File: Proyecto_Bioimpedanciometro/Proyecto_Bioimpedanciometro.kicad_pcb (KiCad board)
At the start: 2 copper layers, 63.5 x 34.3 mm, 28 parts, among them IC1 ATMEGA328P-A, P1 CONN_01X10, P2 CONN_01X04, U1 ADG849, U2 AD8606, U3 APD3339, Y1 Crystal_Small

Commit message: Segunda Version
Empieza PCB
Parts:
- removed C11: C, Capacitors_SMD:C_0805_HandSoldering
- added P3: CONN_01X04, Huellas:Pin_Header_Straight_1x04_Pitch2.54mm_Completo, F.Cu at (175.3, 144.7)
- added R10: R, Resistors_SMD:R_0805_HandSoldering, F.Cu at (175.3, 144.7)
- P1: value CONN_01X10 -> CONN_01X09; footprint Huellas:Pin_Header_Straight_1x10_Pitch2.54mm_Completo -> Huellas:Pin_Header_Straight_1x09_Pitch2.54mm_Completo
- P2: value CONN_01X04 -> CONN_01X03; footprint Huellas:Pin_Header_Straight_1x04_Pitch2.54mm_Completo -> Huellas:Pin_Header_Straight_1x03_Pitch2.54mm_Completo
- moved C7 31.6 mm to (153.7, 111.8), turned to 270 degrees
- moved C9 17.0 mm to (170.9, 111.8), turned to 180 degrees
- moved R9 15.5 mm to (155.4, 128.8)
- moved R7 5.61 mm to (173.5, 127.8)
- moved C4 5.36 mm to (173.5, 125.5)
- moved Y1 4.58 mm to (166.6, 110.2)
- moved IC1 4.33 mm to (159.8, 112.5)
- moved BIO1 4.33 mm to (159.5, 122.2)
- moved P1 2.74 mm to (148.1, 102.9)
- moved C10 1.52 mm to (170.9, 108.7)
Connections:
- C7 pad 1: +3V3 -> /3V3
- C9 pad 1: +3V3 -> GND
- C9 pad 2: GND -> Net-(C9-Pad2)
- IC1 pad 18: +3V3 -> /3V3
- IC1 pad 4: +3V3 -> /3V3
- IC1 pad 6: +3V3 -> /3V3
- IC1 pad 7: Net-(C10-Pad2) -> Net-(C9-Pad2)
- IC1 pad 8: Net-(C11-Pad2) -> Net-(C10-Pad2)
- P1 pad 1: /RXD -> /MOSI
- P1 pad 2: /TXD -> /MISO
- P1 pad 3: /ADC0 -> /SCK
- P1 pad 4: /ADC1 -> /3V3
- P1 pad 5: /ADC2 -> GND
- P1 pad 6: /ADC3 -> /ADC0
- P1 pad 7: /MOSI -> /ADC1
- P1 pad 8: /MISO -> /ADC2
- P1 pad 9: /SCK -> /ADC3
- P2 pad 1: /V_FUENTE -> /RXD
- P2 pad 2: /Z_UK -> /TXD
- P2 pad 3: /IN_A -> /RESET
- Y1 pad 1: Net-(C10-Pad2) -> Net-(C9-Pad2)
- Y1 pad 2: Net-(C11-Pad2) -> Net-(C10-Pad2)
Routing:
- net Net-(C4-Pad2): track 18.1 -> 0.00 mm
- net /VIN_AD5933: track 14.5 -> 0.96 mm
- net GND: track 0.00 -> 10.8 mm
- net /OUT_B: track 10.7 -> 0.00 mm
- net /3V3: track 0.00 -> 7.70 mm
- net /SDA: track 0.00 -> 7.48 mm
- net Net-(BIO1-Pad5): track 6.93 -> 0.00 mm
- net Net-(C9-Pad2): track 0.00 -> 6.44 mm
- net /SCL: track 0.00 -> 6.14 mm
- net Net-(BIO1-Pad4): track 4.45 -> 0.00 mm
- net Net-(BIO1-Pad6): track 3.51 -> 0.00 mm
- net Net-(C11-Pad2): track 3.37 -> 0.00 mm
- net /IN_A: track 3.13 -> 0.00 mm
- net Net-(C10-Pad2): track 3.25 -> 6.12 mm
- net /MISO: track 0.00 -> 1.52 mm

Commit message: Tercera Version
Revisar conexion bajo el micro, se hizo teniendo en cuenta simetria
segun lo hablado.
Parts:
- moved P2 37.2 mm to (167.4, 115.8)
- moved P3 35.3 mm to (203.6, 123.7)
- moved R10 31.2 mm to (196.6, 121.9)
- moved C8 26.8 mm to (171.2, 117.0), turned to 270 degrees
- moved R5 23.7 mm to (173.1, 127.9), turned to 270 degrees
- moved C2 22.4 mm to (181.4, 124.6), turned to 270 degrees
- moved R8 22.1 mm to (170.4, 127.9), turned to 270 degrees
- moved R7 19.8 mm to (153.7, 127.8)
- moved U2 12.6 mm to (176.9, 124.8), turned to 90 degrees
- moved C6 7.82 mm to (173.7, 117.1), turned to 270 degrees
- moved C4 6.56 mm to (167.0, 126.5)
- moved R9 6.37 mm to (152.4, 123.2), turned to 270 degrees
- moved BIO1 0.51 mm to (159.5, 122.7)
- moved C10 0.25 mm to (171.2, 108.7)
- moved C9 0.25 mm to (171.2, 111.8)
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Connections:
- P2 pad 1: /RXD -> /TXD
- P2 pad 2: /TXD -> /RXD
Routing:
- net /VIN_AD5933: track 0.96 -> 20.4 mm
- net Net-(BIO1-Pad6): track 0.00 -> 15.3 mm
- net /MOSI: track 0.00 -> 12.8 mm
- net /3V3: track 7.70 -> 19.6 mm
- net GND: track 10.8 -> 21.8 mm
- net /ADC2: track 0.00 -> 10.8 mm
- net Net-(C4-Pad2): track 0.00 -> 10.3 mm
- net /RESET: track 0.00 -> 10.1 mm
- net /MISO: track 1.52 -> 10.8 mm
- net /ADC1: track 0.00 -> 8.84 mm
- net /SCK: track 0.00 -> 8.42 mm
- net Net-(BIO1-Pad5): track 0.00 -> 8.36 mm
- net /ADC0: track 0.00 -> 8.12 mm
- net /RXD: track 0.00 -> 7.55 mm
- net /TXD: track 0.00 -> 7.12 mm
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
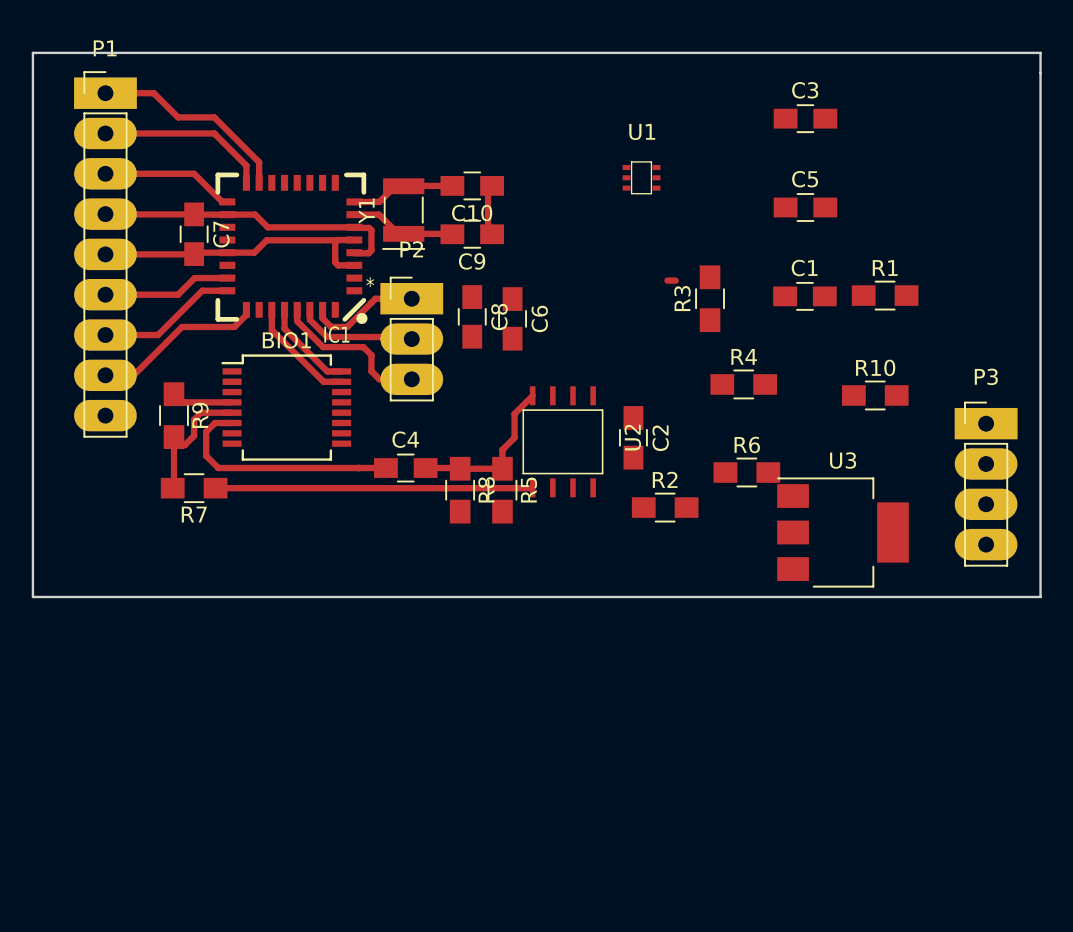
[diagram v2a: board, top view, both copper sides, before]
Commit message: Cuarta Versión
Revisar todo el diseño y errores mas importantes
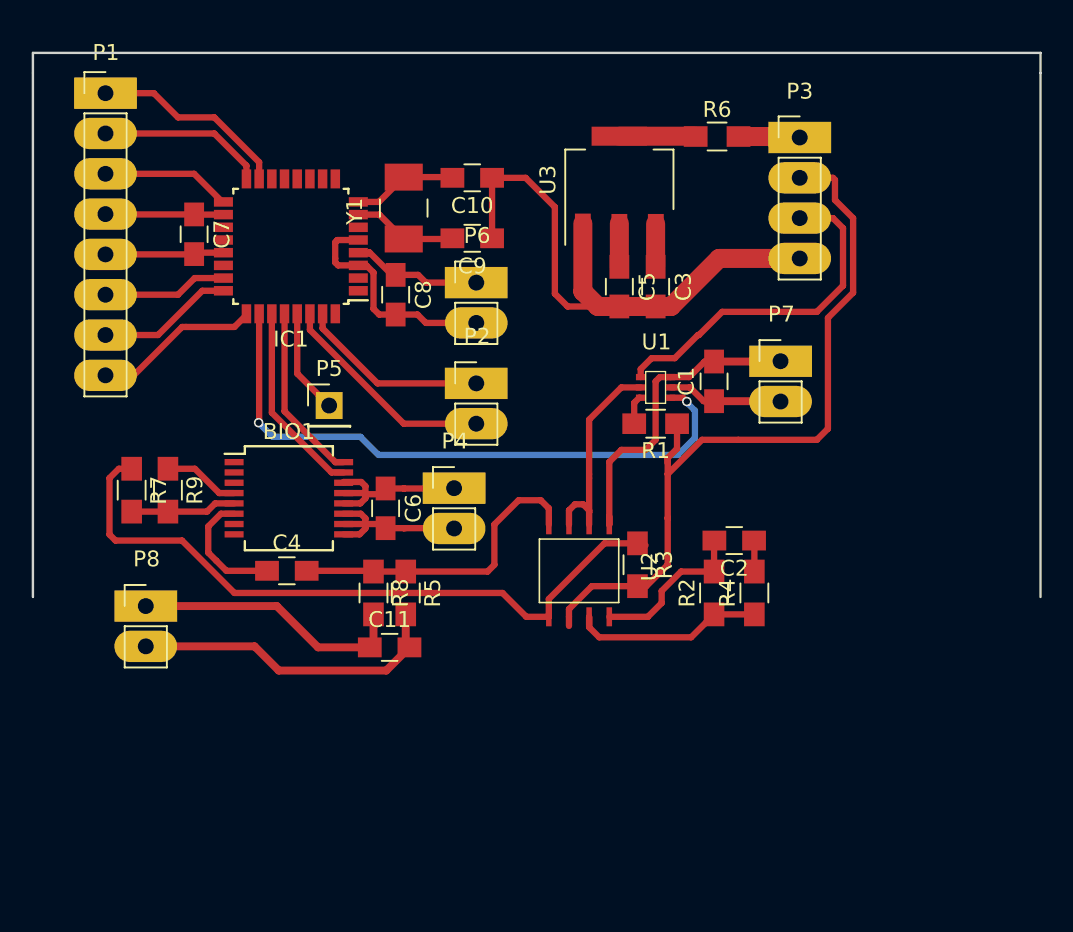
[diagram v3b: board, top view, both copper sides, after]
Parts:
- removed R10: R, Resistors_SMD:R_0805_HandSoldering
- added C11: 0,1uF, Capacitors_SMD:C_0805_HandSoldering, F.Cu at (166.0, 137.8)
- added P4: CONN_01X02, Huellas:Pin_Header_Straight_1x02_Pitch2.54mm_Completo, F.Cu at (170.1, 127.8)
- added P5: CONN_01X01, Pin_Headers:Pin_Header_Straight_1x01_Pitch2.54mm, F.Cu at (162.2, 122.6)
- added P6: CONN_01X02, Huellas:Pin_Header_Straight_1x02_Pitch2.54mm_Completo, F.Cu at (171.4, 114.8)
- added P7: CONN_01X02, Huellas:Pin_Header_Straight_1x02_Pitch2.54mm_Completo, F.Cu at (190.6, 119.8)
- added P8: CONN_01X02, Huellas:Pin_Header_Straight_1x02_Pitch2.54mm_Completo, F.Cu at (150.6, 135.2)
- C1, C2, C7, C8: value C -> 0,1uF
- C10, C9: value C -> 18pF
- C3, C5: value C -> 1uF
- C4: value C -> 47nF
- IC1: footprint Universal:TQFP32 -> Housings_QFP:LQFP-32_7x7mm_Pitch0.8mm
- P1: value CONN_01X09 -> CONN_01X08; footprint Huellas:Pin_Header_Straight_1x09_Pitch2.54mm_Completo -> Huellas:Pin_Header_Straight_1x08_Pitch2.54mm_Completo
- P2: value CONN_01X03 -> CONN_01X02; footprint Huellas:Pin_Header_Straight_1x03_Pitch2.54mm_Completo -> Huellas:Pin_Header_Straight_1x02_Pitch2.54mm_Completo
- R1: value R -> Rcal
- R2, R4, R5, R8: value R -> 50k
- R3: value R -> Rfb
- R6: value R -> 0
- R7, R9: value R -> 20k
- U3: footprint TO_SOT_Packages_SMD:SOT-223 -> Huellas:SOT-223_ADP3339
- Y1: footprint Crystals:Resonator_SMD_muRata_CDSCB-2pin_4.5x2.0mm -> Huellas:AMB3_Crystal_5mm_x_3,2mm_16M
- moved U3 26.3 mm to (180.5, 108.3), turned to 90 degrees
- moved P3 21.5 mm to (191.8, 105.7)
- moved R6 21.3 mm to (186.6, 105.6)
- moved R3 17.4 mm to (181.6, 132.6), turned to 270 degrees
- moved R1 16.6 mm to (182.8, 123.7), turned to 180 degrees
- moved C6 14.4 mm to (165.7, 129.0)
- moved C3 14.2 mm to (182.8, 115.1), turned to 270 degrees
- moved U1 13.2 mm to (182.8, 121.4)
- moved R4 13.2 mm to (189.0, 134.4), turned to 90 degrees
- moved C5 12.7 mm to (180.5, 115.1), turned to 270 degrees
- moved C4 9.90 mm to (159.5, 133.0)
- moved C2 9.07 mm to (187.7, 131.1), turned to 180 degrees
- moved R5 8.89 mm to (167.0, 134.4)
- moved R8 8.47 mm to (165.0, 134.4)
- moved U2 8.19 mm to (177.9, 133.0)
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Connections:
- BIO1 pad 10: +3V3 -> /3V3
- BIO1 pad 11: +3V3 -> /3V3
- BIO1 pad 9: +3V3 -> /3V3
- C1 pad 1: +3V3 -> /3V3
- C2 pad 2: +3V3 -> /3V3
- C5 pad 1: +3V3 -> /3V3
- C6 pad 2: +3V3 -> /3V3
- C8 pad 1: GND -> /3V3
- C8 pad 2: +3V3 -> GND
- P3 pad 2: /Z_UK -> /IN_A
- P3 pad 3: /IN_A -> /Z_UK
- R2 pad 2: +3V3 -> /3V3
- R5 pad 2: +3V3 -> /3V3
- R6 pad 1: +3V3 -> /3V3
- U1 pad 1: /SCL -> /ADC3
- U1 pad 2: +3V3 -> /3V3
- U2 pad 4: +3V3 -> /3V3
- U3 pad 2: +3V3 -> /3V3
- U3 pad 4: (no net) -> /3V3
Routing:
- net GND: track 21.8 -> 109.1 mm
- net /3V3: track 19.6 -> 72.1 mm
- net /IN_A: track 0.00 -> 48.3 mm
- net /ADC3: track 0.00 -> 39.3 mm, vias 0 -> 2
- net /VIN_AD5933: track 20.4 -> 43.3 mm
- net /Z_UK: track 0.00 -> 22.0 mm
- net /OUT_B: track 0.00 -> 13.3 mm
- net Net-(R2-Pad1): track 0.00 -> 12.5 mm
- net Net-(C4-Pad2): track 10.3 -> 19.9 mm
- net Net-(BIO1-Pad6): track 15.3 -> 7.79 mm
- net /RXD: track 7.55 -> 14.2 mm
- net /V_FUENTE: track 0.00 -> 6.62 mm
- net /SDA: track 7.02 -> 12.6 mm
- net /SCL: track 5.90 -> 11.4 mm
- net /TXD: track 7.12 -> 12.3 mm
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
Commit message: Adición del Oscilador con huella y esquematico de medidas personalizadas
Diseño sacado de otros datasheet, con valor de capacitancia recomendado
para la propia referencia
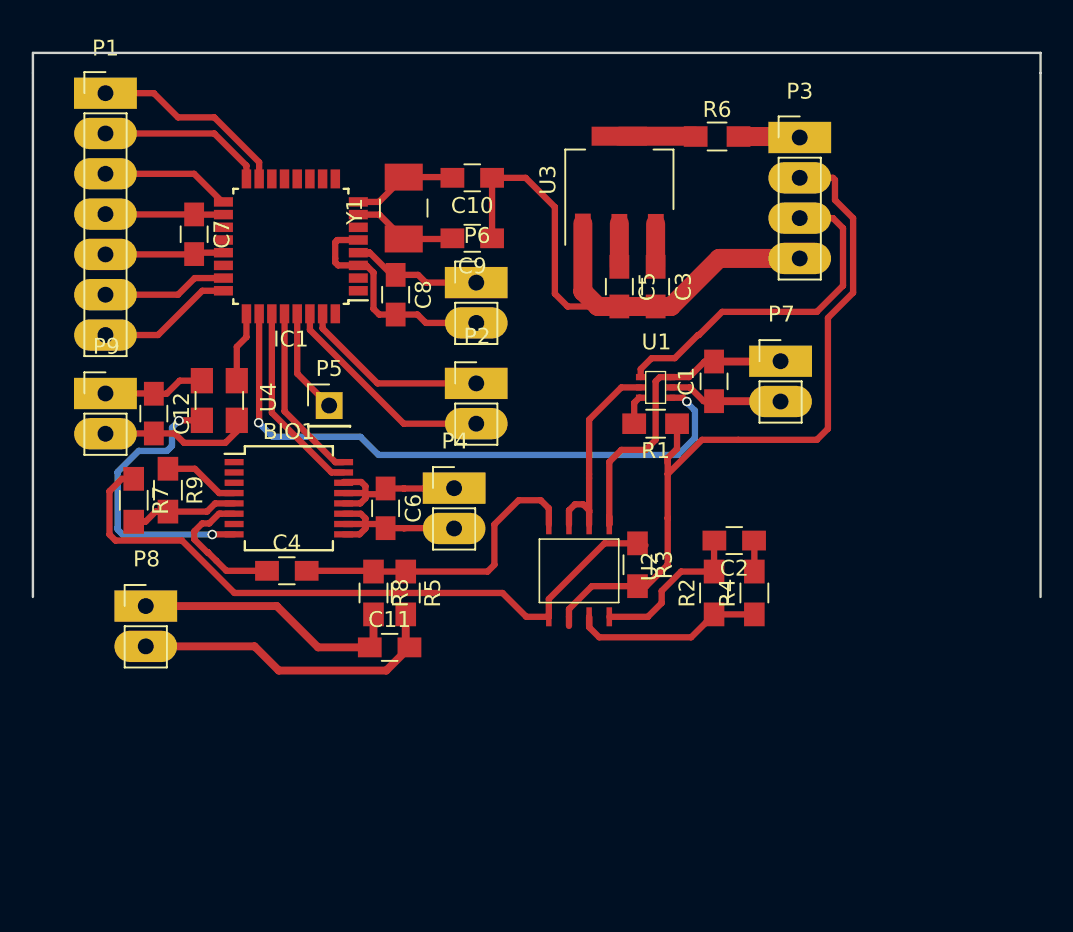
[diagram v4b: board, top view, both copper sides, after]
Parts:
- added C12: 0,01uF, Capacitors_SMD:C_0805_HandSoldering, F.Cu at (151.1, 123.1)
- added P9: CONN_01X02, Huellas:Pin_Header_Straight_1x02_Pitch2.54mm_Completo, F.Cu at (148.1, 121.8)
- added U4: KC5032A_CM, Huellas:KC5032A_CM, F.Cu at (155.3, 122.2)
- P1: value CONN_01X08 -> CONN_01X07; footprint Huellas:Pin_Header_Straight_1x08_Pitch2.54mm_Completo -> Huellas:Pin_Header_Straight_1x07_Pitch2.54mm_Completo
- moved R7 0.65 mm to (149.9, 128.5)
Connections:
- BIO1 pad 8: Net-(BIO1-Pad8) -> /MCLK
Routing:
- net /MCLK: track 0.00 -> 18.4 mm, vias 0 -> 2
- net GND: track 109.1 -> 118.7 mm
- net /3V3: track 72.1 -> 78.6 mm
- net /ADC2: track 10.8 -> 4.79 mm
- net Net-(BIO1-Pad6): track 7.79 -> 8.96 mm
- net /VIN_AD5933: track 43.3 -> 42.7 mm
